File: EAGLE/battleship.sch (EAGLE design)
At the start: 21 parts, among them IC1 EK-TM4C123GXLP

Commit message: update eagle files
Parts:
- added JP10, JP7, JP8, JP9: (no value), pinhead:PINHD-1X10
- added JP11, JP12, JP13: (no value), pinhead:PINHD-2X10
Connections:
- removed net N$3: IC1.+3.3V, JP3.1
- new net 3.3V: IC1.+3.3V, JP1.6, JP10.1, JP2.6, JP3.1, X1-4.KL
- new net CE: JP1.2, JP2.2
- new net CLK: JP1.5, JP2.5
- new net DC: JP1.3, JP2.3
- new net DIN: JP1.4, JP2.4
- new net LIGHT: JP1.7, JP2.7
- new net N$52: JP11.3, JP11.4, JP12.3, JP12.4, JP13.3, JP13.4
- new net N$53: X1-2.KL
- new net N$54: X1-3.KL
- new net N$55: JP11.7, JP11.8, JP12.7, JP12.8, JP13.7, JP13.8
- new net N$58: JP11.11, JP11.12, JP12.11, JP12.12, JP13.11, JP13.12
- new net N$60: JP11.15, JP11.16, JP12.15, JP12.16, JP13.15, JP13.16
- new net N$61: JP11.17, JP11.18, JP12.17, JP12.18, JP13.17, JP13.18
- new net N$62: JP11.19, JP11.20, JP12.19, JP12.20, JP13.19, JP13.20
- new net N$73: JP11.1, JP11.2, JP12.1, JP12.2, JP13.1, JP13.2
- new net N$76: JP11.5, JP11.6, JP12.5, JP12.6, JP13.5, JP13.6
- new net N$77: JP11.10, JP11.9, JP12.10, JP12.9, JP13.10, JP13.9
- new net N$79: JP11.13, JP11.14, JP12.13, JP12.14, JP13.13, JP13.14
- new net RESET: JP1.1, JP2.1
- net GND: now also JP1.8, JP2.8, JP7.1, JP9.2, X1-1.KL
- net N$10: now also JP10.10
- net N$11: now also JP7.10
- net N$12: now also JP7.9
- net N$13: now also JP7.8
- net N$14: now also JP7.7
- net N$15: now also JP7.6
- net N$16: now also JP7.5
- net N$17: now also JP7.4
- net N$18: now also JP7.3
- net N$19: now also JP7.2
- net N$21: now also JP9.1
- net N$23: now also JP9.3
- net N$24: now also JP9.4
- net N$25: now also JP9.8
- net N$26: now also JP9.9
- net N$27: now also JP9.10
- net N$28: now also JP8.10
- net N$29: now also JP8.9
- net N$30: now also JP8.8
- net N$31: now also JP8.7
- net N$32: now also JP8.6
- net N$33: now also JP8.5
- net N$34: now also JP8.4
- net N$35: now also JP8.3
- net N$36: now also JP8.2
- net N$37: now also JP8.1
- net N$38: now also JP10.6
- net N$39: now also JP9.7
- net N$4: now also JP10.2
- net N$40: now also JP10.7
- net N$41: now also JP9.6
- net N$42: now also JP9.5
- net N$5: now also JP10.3
- net N$6: now also JP10.4
- net N$7: now also JP10.5
- net N$8: now also JP10.8
- net N$9: now also JP10.9
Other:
- moved on the sheet: JP3, JP6

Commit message: update eagle files
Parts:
- removed JP10, JP6, JP7, JP8, JP9: (no value), pinhead:PINHD-1X10
- added JP14: (no value), pinhead:PINHD-2X10
- JP3, JP4, JP5: device pinhead:PINHD-1X10 -> pinhead:PINHD-2X10
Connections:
- net N$51 renamed BUZZERPIN
- removed net N$1: LEFT.3, LEFT.4
- removed net N$10: IC1.PA7, JP10.10, JP3.10
- removed net N$11: IC1.PA2, JP6.10, JP7.10
- removed net N$12: IC1.PA3, JP6.9, JP7.9
- removed net N$13: IC1.PA4, JP6.8, JP7.8
- removed net N$14: IC1.PB6, JP6.7, JP7.7
- removed net N$15: IC1.PB7, JP6.6, JP7.6
- removed net N$16: IC1.RESET, JP6.5, JP7.5
- removed net N$2: LEFT.1, LEFT.2, R1.1
- removed net N$20: RIGHT.3, RIGHT.4
- removed net N$22: R2.1, RIGHT.1, RIGHT.2
- removed net N$28: IC1.PF4, JP5.10, JP8.10
- removed net N$29: IC1.PD7, JP5.9, JP8.9
- removed net N$30: IC1.PD6, JP5.8, JP8.8
- removed net N$35: IC1.PB3, JP5.3, JP8.3
- removed net N$4: IC1.PB5, JP10.2, JP3.2
- removed net N$43: DOWN.3, DOWN.4
- removed net N$44: DOWN.1, DOWN.2, R3.1
- removed net N$45: UP.3, UP.4
- removed net N$46: R4.1, UP.1, UP.2
- removed net N$47: SELECT.3, SELECT.4
- removed net N$48: R5.1, SELECT.1, SELECT.2
- removed net N$49: BACK.3, BACK.4
- removed net N$5: IC1.PB0, JP10.3, JP3.3
- removed net N$50: BACK.1, BACK.2, R6.1
- removed net N$6: IC1.PB1, JP10.4, JP3.4
- removed net N$7: IC1.PE4, JP10.5, JP3.5
- removed net N$8: IC1.PA5, JP10.8, JP3.8
- removed net N$9: IC1.PA6, JP10.9, JP3.9
- new net BACKSIG: BACK.1, BACK.2, IC1.PB1, JP14.7, JP14.8, R6.1
- new net BUZZER: IC1.PA4, JP5.15, JP5.16
- new net DOWNSIG: DOWN.1, DOWN.2, IC1.PB6, JP5.13, JP5.14, R3.1
- new net LEFTSIG: IC1.PB5, JP14.3, JP14.4, LEFT.1, LEFT.2, R1.1
- new net N$56: IC1.PD6, JP4.15, JP4.16
- new net N$57: IC1.PC7, JP4.13, JP4.14
- new net N$59: IC1.PC6, JP4.11, JP4.12
- new net N$63: IC1.PC5, JP4.10, JP4.9
- new net N$64: IC1.PC4, JP4.7, JP4.8
- new net N$65: IC1.PB3, JP4.5, JP4.6
- new net N$66: IC1.PF3, JP4.3, JP4.4
- new net N$67: IC1.PF2, JP4.1, JP4.2
- new net N$68: IC1.PE5, JP14.11, JP14.12
- new net N$69: IC1.PE1, JP3.13, JP3.14
- new net RIGHTSIG: IC1.PB7, JP5.11, JP5.12, R2.1, RIGHT.1, RIGHT.2
- new net SELECTSIG: IC1.PB0, JP14.5, JP14.6, R5.1, SELECT.1, SELECT.2
- new net UPSIG: IC1.PB4, JP14.13, JP14.14, R4.1, UP.1, UP.2
- net 3.3V: now also BACK.3, BACK.4, DOWN.3, DOWN.4, JP14.1, JP14.2, LEFT.3, LEFT.4, RIGHT.3, RIGHT.4, SELECT.3, SELECT.4, UP.3, UP.4; no longer JP10.1, JP3.1
- net GND: now also JP3.3, JP3.4, JP5.1, JP5.2; no longer JP4.2, JP6.1, JP7.1, JP9.2
- net N$17: now also IC1.PE4, JP14.10, JP14.9; no longer IC1.PF0, JP6.4, JP7.4
- net N$18: now also IC1.PA5, JP14.15, JP14.16; no longer IC1.PE0, JP6.3, JP7.3
- net N$19: now also IC1.PA6, JP14.17, JP14.18; no longer IC1.PB2, JP6.2, JP7.2
- net N$21: now also JP3.1, JP3.2; no longer JP4.1, JP9.1
- net N$23: now also JP3.5, JP3.6; no longer JP4.3, JP9.3
- net N$24: now also JP3.7, JP3.8; no longer JP4.4, JP9.4
- net N$25: now also IC1.PA7, JP14.19, JP14.20; no longer IC1.PE2, JP4.8, JP9.8
- net N$26: now also IC1.PA2, JP5.19, JP5.20; no longer IC1.PE3, JP4.9, JP9.9
- net N$27: now also IC1.PA3, JP5.17, JP5.18; no longer IC1.PF1, JP4.10, JP9.10
- net N$31: now also IC1.RESET, JP5.10, JP5.9; no longer IC1.PC7, JP5.7, JP8.7
- net N$32: now also IC1.PF0, JP5.7, JP5.8; no longer IC1.PC6, JP5.6, JP8.6
- net N$33: now also IC1.PE0, JP5.6; no longer IC1.PC5, JP8.5
- net N$34: now also IC1.PB2, JP5.3; no longer IC1.PC4, JP8.4
- net N$36: now also IC1.PE2, JP3.15, JP3.16; no longer IC1.PF3, JP5.2, JP8.2
- net N$37: now also IC1.PE3, JP3.17, JP3.18; no longer IC1.PF2, JP5.1, JP8.1
- net N$38: now also IC1.PF1, JP3.19, JP3.20; no longer IC1.PE5, JP10.6, JP3.6
- net N$39: now also IC1.PF4, JP4.19, JP4.20; no longer IC1.PE1, JP4.7, JP9.7
- net N$40: now also IC1.PD7, JP4.17, JP4.18; no longer IC1.PB4, JP10.7, JP3.7
- net N$41: now also JP3.11, JP3.12; no longer JP4.6, JP9.6
- net N$42: now also JP3.10, JP3.9; no longer JP4.5, JP9.5

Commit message: finished board
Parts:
- added R7: 330, rcl:R-US_0207/10
- added SJ1, SJ2: (no value), jumper:SJ
- JP1, JP2: value (none) -> Display
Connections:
- removed net BUZZER: IC1.PA4, JP5.15, JP5.16
- removed net N$18: IC1.PA5, JP14.15, JP14.16
- removed net N$19: IC1.PA6, JP14.17, JP14.18
- removed net N$25: IC1.PA7, JP14.19, JP14.20
- removed net N$26: IC1.PA2, JP5.19, JP5.20
- removed net N$27: IC1.PA3, JP5.17, JP5.18
- removed net N$53: X1-2.KL
- removed net N$54: X1-3.KL
- removed net N$63: IC1.PC5, JP4.10, JP4.9
- removed net N$64: IC1.PC4, JP4.7, JP4.8
- new net BL: JP1.7, JP2.7, R7.2
- new net RX: IC1.PC4, JP4.7, JP4.8, X1-2.KL
- new net TX: IC1.PC5, JP4.10, JP4.9, X1-3.KL
- net BUZZERPIN: now also IC1.PA4, JP5.15, JP5.16
- net CE: now also IC1.PA3, JP5.17, JP5.18
- net CLK: now also IC1.PA2, JP5.19, JP5.20
- net DC: now also IC1.PA6, JP14.17, JP14.18
- net DIN: now also IC1.PA5, JP14.15, JP14.16
- net GND: now also SJ1.1
- net LIGHT: now also R7.1, SJ1.2, SJ2.2; no longer JP1.7, JP2.7
- net N$34: now also SJ2.1
- net RESET: now also IC1.PA7, JP14.19, JP14.20

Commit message: edit boards
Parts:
- added SJ3, SJ4: (no value), jumper:SJ
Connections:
- net BL: now also SJ3.2, SJ4.1
- net GND: now also SJ3.1
- net LIGHT: now also SJ4.2
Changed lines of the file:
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@@
 <part name="SJ2" library="jumper" library_urn="urn:adsk.eagle:library:252" deviceset="SJ" device="" package3d_urn="urn:adsk.eagle:package:15471/1"/>
 <part name="R7" library="rcl" library_urn="urn:adsk.eagle:library:334" deviceset="R-US_" device="0207/10" package3d_urn="urn:adsk.eagle:package:23491/1" value="330"/>
+<part name="SJ3" library="jumper" library_urn="urn:adsk.eagle:library:252" deviceset="SJ" device="" package3d_urn="urn:adsk.eagle:package:15471/1"/>
+<part name="SJ4" library="jumper" library_urn="urn:adsk.eagle:library:252" deviceset="SJ" device="" package3d_urn="urn:adsk.eagle:package:15471/1"/>
 </parts>
 <sheets>
@@
 <attribute name="NAME" x="219.71" y="80.2386" size="1.778" layer="95"/>
 <attribute name="VALUE" x="219.71" y="75.438" size="1.778" layer="96"/>
+</instance>
+<instance part="SJ3" gate="1" x="177.8" y="71.12">
+<attribute name="NAME" x="175.26" y="73.66" size="1.778" layer="95"/>
+<attribute name="VALUE" x="175.26" y="67.31" size="1.778" layer="96"/>
+</instance>
+<instance part="SJ4" gate="1" x="198.12" y="73.66" rot="R90">
+<attribute name="NAME" x="195.58" y="71.12" size="1.778" layer="95" rot="R90"/>
+<attribute name="VALUE" x="201.93" y="71.12" size="1.778" layer="96" rot="R90"/>
 </instance>
 </instances>
@@
 <segment>
 <pinref part="SJ1" gate="1" pin="1"/>
-<wire x1="172.72" y1="78.74" x2="162.56" y2="78.74" width="0.1524" layer="91"/>
+<wire x1="172.72" y1="78.74" x2="167.64" y2="78.74" width="0.1524" layer="91"/>
 <label x="162.56" y="78.74" size="1.778" layer="95"/>
+<pinref part="SJ3" gate="1" pin="1"/>
+<wire x1="167.64" y1="78.74" x2="162.56" y2="78.74" width="0.1524" layer="91"/>
+<wire x1="172.72" y1="71.12" x2="167.64" y2="71.12" width="0.1524" layer="91"/>
+<wire x1="167.64" y1="71.12" x2="160.02" y2="71.12" width="0.1524" layer="91"/>
+<wire x1="167.64" y1="71.12" x2="167.64" y2="78.74" width="0.1524" layer="91"/>
+<junction x="167.64" y="71.12"/>
+<junction x="167.64" y="78.74"/>
 </segment>
 </net>
@@
 <segment>
 <pinref part="SJ1" gate="1" pin="2"/>
-<wire x1="182.88" y1="78.74" x2="193.04" y2="78.74" width="0.1524" layer="91"/>
 <label x="187.96" y="78.74" size="1.778" layer="95"/>
+<pinref part="R7" gate="G$1" pin="1"/>
+<label x="203.2" y="78.74" size="1.778" layer="95"/>
+<wire x1="182.88" y1="78.74" x2="198.12" y2="78.74" width="0.1524" layer="91"/>
+<pinref part="SJ4" gate="1" pin="2"/>
+<wire x1="198.12" y1="78.74" x2="218.44" y2="78.74" width="0.1524" layer="91"/>
+<junction x="198.12" y="78.74"/>
 </segment>
 <segment>
@@
 <wire x1="142.24" y1="38.1" x2="149.86" y2="38.1" width="0.1524" layer="91"/>
 <label x="142.24" y="38.1" size="1.778" layer="95"/>
-</segment>
-<segment>
-<pinref part="R7" gate="G$1" pin="1"/>
-<wire x1="218.44" y1="78.74" x2="203.2" y2="78.74" width="0.1524" layer="91"/>
-<label x="203.2" y="78.74" size="1.778" layer="95"/>
 </segment>
 </net>
@@
 </segment>
 <segment>
+<pinref part="SJ3" gate="1" pin="2"/>
 <pinref part="R7" gate="G$1" pin="2"/>
-<wire x1="228.6" y1="78.74" x2="251.46" y2="78.74" width="0.1524" layer="91"/>
+<wire x1="228.6" y1="78.74" x2="241.3" y2="78.74" width="0.1524" layer="91"/>
 <label x="243.84" y="78.74" size="1.778" layer="95"/>
-</segment>
-</net>
+<wire x1="241.3" y1="78.74" x2="251.46" y2="78.74" width="0.1524" layer="91"/>
+<wire x1="182.88" y1="71.12" x2="193.04" y2="71.12" width="0.1524" layer="91"/>
+<wire x1="193.04" y1="71.12" x2="241.3" y2="71.12" width="0.1524" layer="91"/>
+<wire x1="241.3" y1="71.12" x2="241.3" y2="78.74" width="0.1524" layer="91"/>
+<junction x="241.3" y="78.74"/>
+<wire x1="193.04" y1="71.12" x2="193.04" y2="68.58" width="0.1524" layer="91"/>
+<junction x="193.04" y="71.12"/>
+<pinref part="SJ4" gate="1" pin="1"/>
+<wire x1="193.04" y1="68.58" x2="198.12" y2="68.58" width="0.1524" layer="91"/>
+</segment>
+</net>

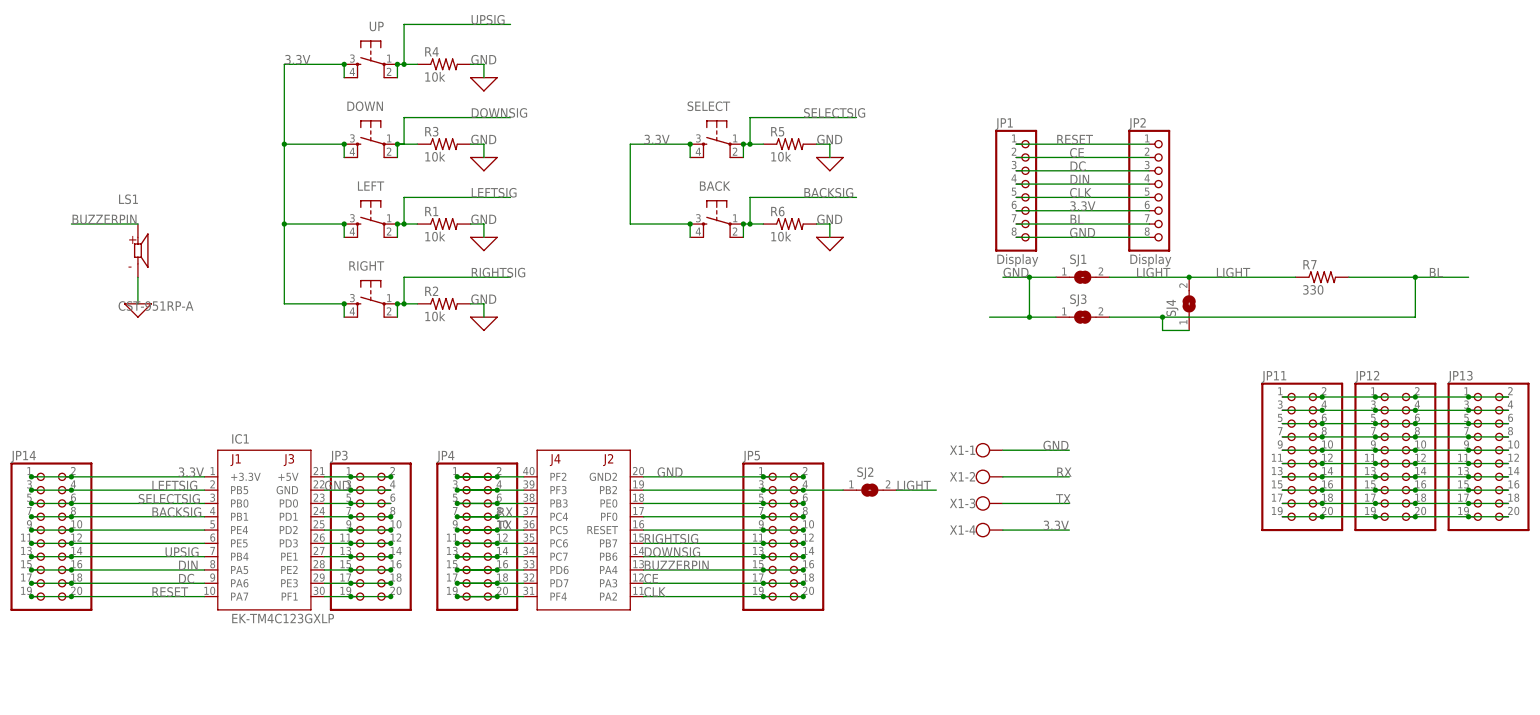
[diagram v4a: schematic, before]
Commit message: reduced PCB size
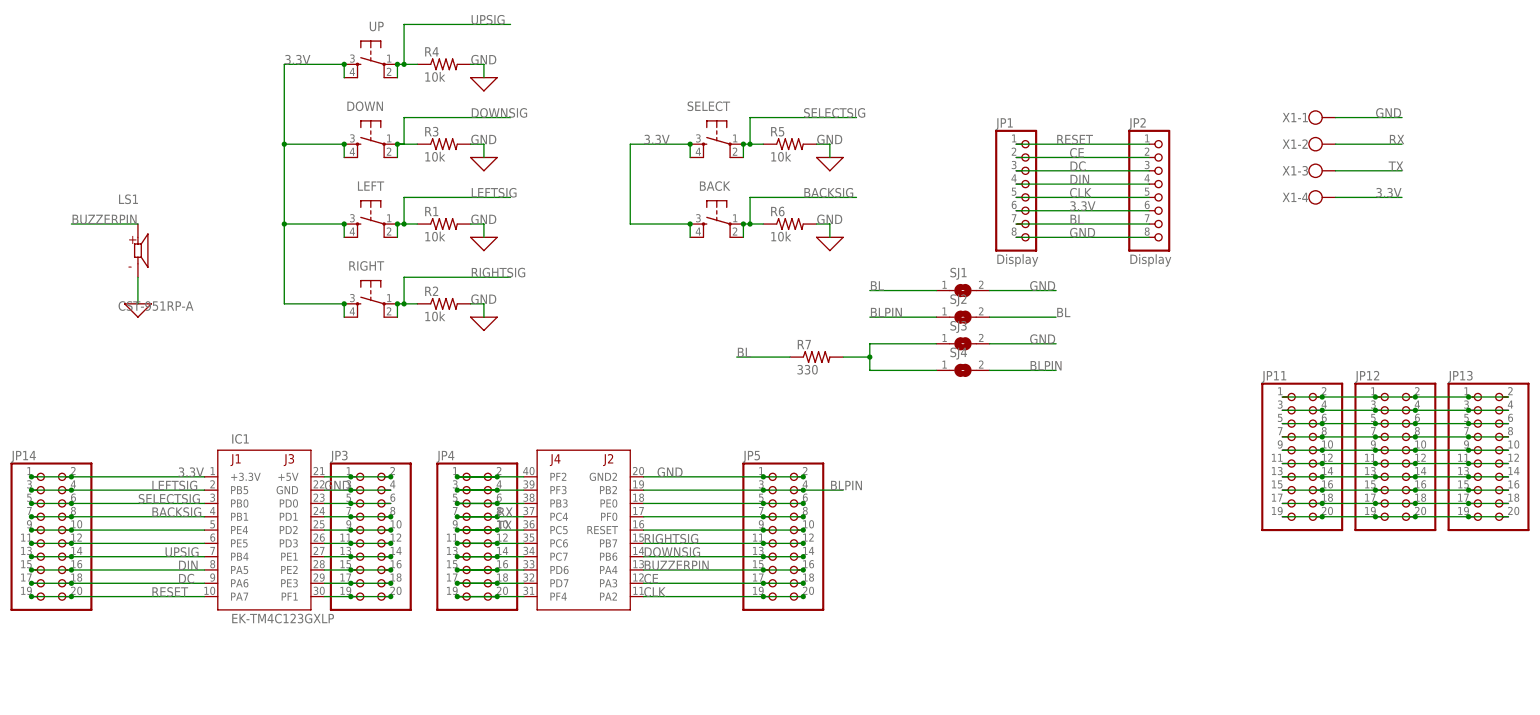
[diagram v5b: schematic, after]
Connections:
- removed net LIGHT: R7.1, SJ1.2, SJ2.2, SJ4.2
- removed net N$34: IC1.PB2, JP5.3, JP5.4, SJ2.1
- new net BLPIN: IC1.PB2, JP5.3, JP5.4, SJ2.1, SJ4.2
- new net N$6: R7.2, SJ3.1, SJ4.1
- net BL: now also R7.1, SJ1.1, SJ2.2; no longer R7.2, SJ3.2, SJ4.1
- net GND: now also SJ1.2, SJ3.2; no longer SJ1.1, SJ3.1
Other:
- moved on the sheet: R7, SJ1, SJ2, SJ3, SJ4, X1-1, X1-2, X1-3, X1-4

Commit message: update board and dxf
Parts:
- added JP6: (no value), pinhead:PINHD-2X10
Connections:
- new net N$1: JP6.1, JP6.2
- new net N$10: JP6.19, JP6.20
- new net N$11: JP6.17, JP6.18
- new net N$2: JP6.3, JP6.4
- new net N$3: JP6.5, JP6.6
- new net N$4: JP6.7, JP6.8
- new net N$5: JP6.10, JP6.9
- new net N$7: JP6.11, JP6.12
- new net N$8: JP6.13, JP6.14
- new net N$9: JP6.15, JP6.16
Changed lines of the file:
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@@
 <part name="SJ4" library="jumper" library_urn="urn:adsk.eagle:library:252" deviceset="SJ" device="" package3d_urn="urn:adsk.eagle:package:15471/1"/>
 <part name="R7" library="rcl" library_urn="urn:adsk.eagle:library:334" deviceset="R-US_" device="0207/10" package3d_urn="urn:adsk.eagle:package:23491/1" value="330"/>
+<part name="JP6" library="pinhead" library_urn="urn:adsk.eagle:library:325" deviceset="PINHD-2X10" device="" package3d_urn="urn:adsk.eagle:package:22405/2"/>
 </parts>
 <sheets>
@@
 <attribute name="NAME" x="123.19" y="64.9986" size="1.778" layer="95"/>
 <attribute name="VALUE" x="123.19" y="60.198" size="1.778" layer="96"/>
+</instance>
+<instance part="JP6" gate="A" x="218.44" y="12.7">
+<attribute name="NAME" x="212.09" y="26.035" size="1.778" layer="95"/>
+<attribute name="VALUE" x="212.09" y="-5.08" size="1.778" layer="96"/>
 </instance>
 </instances>
@@
 </segment>
 </net>
+<net name="N$1" class="0">
+<segment>
+<pinref part="JP6" gate="A" pin="1"/>
+<pinref part="JP6" gate="A" pin="2"/>
+<wire x1="215.9" y1="22.86" x2="223.52" y2="22.86" width="0.1524" layer="91"/>
+</segment>
+</net>
+<net name="N$2" class="0">
+<segment>
+<pinref part="JP6" gate="A" pin="4"/>
+<pinref part="JP6" gate="A" pin="3"/>
+<wire x1="223.52" y1="20.32" x2="215.9" y2="20.32" width="0.1524" layer="91"/>
+</segment>
+</net>
+<net name="N$3" class="0">
+<segment>
+<pinref part="JP6" gate="A" pin="5"/>
+<pinref part="JP6" gate="A" pin="6"/>
+<wire x1="215.9" y1="17.78" x2="223.52" y2="17.78" width="0.1524" layer="91"/>
+</segment>
+</net>
+<net name="N$4" class="0">
+<segment>
+<pinref part="JP6" gate="A" pin="8"/>
+<pinref part="JP6" gate="A" pin="7"/>
+<wire x1="223.52" y1="15.24" x2="215.9" y2="15.24" width="0.1524" layer="91"/>
+</segment>
+</net>
+<net name="N$5" class="0">
+<segment>
+<pinref part="JP6" gate="A" pin="9"/>
+<pinref part="JP6" gate="A" pin="10"/>
+<wire x1="215.9" y1="12.7" x2="223.52" y2="12.7" width="0.1524" layer="91"/>
+</segment>
+</net>
+<net name="N$7" class="0">
+<segment>
+<pinref part="JP6" gate="A" pin="12"/>
+<pinref part="JP6" gate="A" pin="11"/>
+<wire x1="223.52" y1="10.16" x2="215.9" y2="10.16" width="0.1524" layer="91"/>
+</segment>
+</net>
+<net name="N$8" class="0">
+<segment>
+<pinref part="JP6" gate="A" pin="13"/>
+<pinref part="JP6" gate="A" pin="14"/>
+<wire x1="215.9" y1="7.62" x2="223.52" y2="7.62" width="0.1524" layer="91"/>
+</segment>
+</net>
+<net name="N$9" class="0">
+<segment>
+<pinref part="JP6" gate="A" pin="16"/>
+<pinref part="JP6" gate="A" pin="15"/>
+<wire x1="223.52" y1="5.08" x2="215.9" y2="5.08" width="0.1524" layer="91"/>
+</segment>
+</net>
+<net name="N$10" class="0">
+<segment>
+<pinref part="JP6" gate="A" pin="19"/>
+<pinref part="JP6" gate="A" pin="20"/>
+<wire x1="215.9" y1="0" x2="223.52" y2="0" width="0.1524" layer="91"/>
+</segment>
+</net>
+<net name="N$11" class="0">
+<segment>
+<pinref part="JP6" gate="A" pin="18"/>
+<pinref part="JP6" gate="A" pin="17"/>
+<wire x1="223.52" y1="2.54" x2="215.9" y2="2.54" width="0.1524" layer="91"/>
+</segment>
+</net>

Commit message: minor board updates
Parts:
- renumbered JP1 to DISPLAY, JP2 to DISPLAY2
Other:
- moved on the sheet: IC1, JP14, JP3, JP4, JP5, LS1
